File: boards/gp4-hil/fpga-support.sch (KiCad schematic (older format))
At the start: 0 parts

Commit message: Continued work on gp4-hil board schematic
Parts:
- added U2: XC7A100T-1FTG256C, symbol XC7AxT-xFTG256x
- added U6: W25Q32FW, symbol W25Q80BV
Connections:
- new net: U2.A16 (VCCO_15), U2.B13 (VCCO_15), U2.C10 (VCCO_15), U2.E14 (VCCO_15), U2.H15 (VCCO_15), U2.J12 (VCCO_15)
- new net: U2.A6 (VCCO_35), U2.B3 (VCCO_35), U2.D7 (VCCO_35), U2.E4 (VCCO_35), U2.F1 (VCCO_35), U2.J2 (VCCO_35)
- new net: U2.E10 (VCCBRAM), U2.F11 (VCCBRAM)
- new net: U2.F7 (VCCINT), U2.F9 (VCCINT), U2.G6 (VCCINT), U2.H9 (VCCINT), U2.J6 (VCCINT), U2.K9 (VCCINT), U2.L8 (VCCINT)
- new net: U2.G10 (VCCAUX), U2.J10 (VCCAUX), U2.K11 (VCCAUX), U2.L10 (VCCAUX)
- new net: U2.L16 (VCCO_14), U2.M13 (VCCO_14), U2.N10 (VCCO_14), U2.P7 (VCCO_14), U2.R14 (VCCO_14), U2.T11 (VCCO_14)
- new net: U2.M3 (VCCO_34), U2.R4 (VCCO_34), U2.T1 (VCCO_34)
- new net GND: U2.A1 (GND), U2.A11 (GND), U2.B8 (GND), U2.C15 (GND), U2.C5 (GND), U2.D12 (GND), U2.D2 (GND), U2.E9 (GND), U2.F10 (GND), U2.F16 (GND), U2.F6 (GND), U2.G13 (GND), U2.G3 (GND), U2.G7 (GNDADC), U2.G9 (GND), U2.H6 (GND), U2.J11 (GND), U2.J9 (GND), U2.K14 (GND), U2.K4 (GND), U2.K6 (GND), U2.L1 (GND), U2.L11 (GND), U2.M8 (GND), U2.N15 (GND), U2.N5 (GND), U2.P12 (GND), U2.P2 (GND), U2.R9 (GND), U2.T16 (GND), U2.T6 (GND)
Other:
- note added: "Recommended decoupling for 7a100t (largest FTG256 device):\n\nVCCINT\n* 1x 330 uF\n* 6x 4.7 uF\n* 8x 0.47 uF\n\nVCCBRAM\n* 1x 100 uF\n* 2x 0.47 uF\n\nVCCAUX\n* 1x 47 uF \n* 2x 4.7 uF \n* 3x 0.47 uF\n\nVCCO_0\n* 1x 47 uF\n\nVCCO (per bank):\n* 1x 47/100 uF per 4 banks\n* 2x 4.7 uF\n* 4x 0.47 uF"
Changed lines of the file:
@@
 EELAYER 25 0
 EELAYER END
-$Descr A4 11693 8268
+$Descr A3 16535 11693
 encoding utf-8
-Sheet 1 7
+Sheet 7 7
 Title ""
-Date ""
+Date "2016-05-10"
 Rev ""
 Comp ""
@@
 Comment4 ""
 $EndDescr
+$Comp
+L XC7AxT-xFTG256x U2
+U 1 1 5732CCFA
+P 1900 6200
+F 0 "U2" H 1900 6000 60  0000 L CNN
+F 1 "XC7A100T-1FTG256C" H 1900 6100 60  0000 L CNN
+F 2 "" H 1900 6200 60  0000 C CNN
+F 3 "" H 1900 6200 60  0000 C CNN
+	1    1900 6200
+	1    0    0    -1
+$EndComp
+$Comp
+L XC7AxT-xFTG256x U2
+U 2 1 5732CEE7
+P 5300 6200
+F 0 "U2" H 5300 6000 60  0000 L CNN
+F 1 "XC7A100T-1FTG256C" H 5300 6100 60  0000 L CNN
+F 2 "" H 5300 6200 60  0000 C CNN
+F 3 "" H 5300 6200 60  0000 C CNN
+	2    5300 6200
+	1    0    0    -1
+$EndComp
+$Comp
+L W25Q80BV U6
+U 1 1 5732D74D
+P 12400 4150
+F 0 "U6" H 12400 4837 60  0000 C CNN
+F 1 "W25Q32FW" H 12400 4731 60  0000 C CNN
+F 2 "" H 12400 4150 60  0000 C CNN
+F 3 "" H 12400 4150 60  0000 C CNN
+	1    12400 4150
+	1    0    0    -1
+$EndComp
+Text Notes 7450 9100 0    60   ~ 0
+Recommended decoupling for 7a100t (largest FTG256 device):\n\nVCCINT\n* 1x 330 uF\n* 6x 4.7 uF\n* 8x 0.47 uF\n\nVCCBRAM\n* 1x 100 uF\n* 2x 0.47 uF\n\nVCCAUX\n* 1x 47 uF \n* 2x 4.7 uF \n* 3x 0.47 uF\n\nVCCO_0\n* 1x 47 uF\n\nVCCO (per bank):\n* 1x 47/100 uF per 4 banks\n* 2x 4.7 uF\n* 4x 0.47 uF
+Wire Wire Line
+	5100 1500 5000 1500
+Wire Wire Line
+	5000 1300 5000 4400
+Wire Wire Line
+	5000 1600 5100 1600
+Wire Wire Line
+	5000 1700 5100 1700
+Connection ~ 5000 1600
+Wire Wire Line
+	5000 1800 5100 1800
+Connection ~ 5000 1700
+Wire Wire Line
+	5000 1900 5100 1900
+Connection ~ 5000 1800
+Wire Wire Line
+	5000 2000 5100 2000
+Connection ~ 5000 1900
+Wire Wire Line
+	5000 2100 5100 2100
+Connection ~ 5000 2000
+Wire Wire Line
+	5000 2200 5100 2200
+Connection ~ 5000 2100
+Wire Wire Line
+	5000 2300 5100 2300
+Connection ~ 5000 2200
+Wire Wire Line
+	5000 2400 5100 2400
+Connection ~ 5000 2300
+Wire Wire Line
+	5000 2500 5100 2500
+Connection ~ 5000 2400
+Wire Wire Line
+	5000 2600 5100 2600
+Connection ~ 5000 2500
+Wire Wire Line
+	5000 2700 5100 2700
+Connection ~ 5000 2600
+Wire Wire Line
+	5000 2800 5100 2800
+Connection ~ 5000 2700
+Wire Wire Line
+	5000 2900 5100 2900
+Connection ~ 5000 2800
+Wire Wire Line
+	5000 3000 5100 3000
+Connection ~ 5000 2900
+Wire Wire Line
+	5000 3100 5100 3100
+Connection ~ 5000 3000
+Wire Wire Line
+	5000 3200 5100 3200
+Connection ~ 5000 3100
+Wire Wire Line
+	5000 3300 5100 3300
+Connection ~ 5000 3200
+Wire Wire Line
+	5000 3400 5100 3400
+Connection ~ 5000 3300
+Wire Wire Line
+	5000 3500 5100 3500
+Connection ~ 5000 3400
+Wire Wire Line
+	5000 3600 5100 3600
+Connection ~ 5000 3500
+Wire Wire Line
+	5000 3700 5100 3700
+Connection ~ 5000 3600
+Wire Wire Line
+	5000 3800 5100 3800
+Connection ~ 5000 3700
+Wire Wire Line
+	5000 3900 5100 3900
+Connection ~ 5000 3800
+Wire Wire Line
+	5000 4000 5100 4000
+Connection ~ 5000 3900
+Wire Wire Line
+	5000 4100 5100 4100
+Connection ~ 5000 4000
+Wire Wire Line
+	5000 4200 5100 4200
+Connection ~ 5000 4100
+Wire Wire Line
+	5000 4300 5100 4300
+Connection ~ 5000 4200
+Wire Wire Line
+	5000 4400 5100 4400
+Connection ~ 5000 4300
+Wire Wire Line
+	4850 1300 5100 1300
+Connection ~ 5000 1500
+Connection ~ 5000 1300
+Wire Wire Line
+	6850 1650 6950 1650
+Wire Wire Line
+	6950 1650 6950 2250
+Wire Wire Line
+	6950 1750 6850 1750
+Wire Wire Line
+	6950 1850 6850 1850
+Connection ~ 6950 1750
+Wire Wire Line
+	6950 1950 6850 1950
+Connection ~ 6950 1850
+Wire Wire Line
+	6950 2050 6850 2050
+Connection ~ 6950 1950
+Wire Wire Line
+	6950 2150 6850 2150
+Connection ~ 6950 2050
+Wire Wire Line
+	6950 2250 6850 2250
+Connection ~ 6950 2150
+Wire Wire Line
+	6850 2450 6950 2450
+Wire Wire Line
+	6950 2450 6950 2550
+Wire Wire Line
+	6950 2550 6850 2550
+Wire Wire Line
+	6850 2750 6950 2750
+Wire Wire Line
+	6950 2750 6950 3050
+Wire Wire Line
+	6950 2850 6850 2850
+Wire Wire Line
+	6950 2950 6850 2950
+Connection ~ 6950 2850
+Wire Wire Line
+	6950 3050 6850 3050
+Connection ~ 6950 2950
+Wire Wire Line
+	6850 3450 6950 3450
+Wire Wire Line
+	6950 3450 6950 3950
+Wire Wire Line
+	6950 3550 6850 3550
+Wire Wire Line
+	6950 3650 6850 3650
+Connection ~ 6950 3550
+Wire Wire Line
+	6950 3750 6850 3750
+Connection ~ 6950 3650
+Wire Wire Line
+	6950 3850 6850 3850
+Connection ~ 6950 3750
+Wire Wire Line
+	6950 3950 6850 3950
+Connection ~ 6950 3850
+Wire Wire Line
+	6850 4150 6950 4150
+Wire Wire Line
+	6950 4150 6950 4650
+Wire Wire Line
+	6950 4250 6850 4250
+Wire Wire Line
+	6950 4350 6850 4350
+Connection ~ 6950 4250
+Wire Wire Line
+	6950 4450 6850 4450
+Connection ~ 6950 4350
+Wire Wire Line
+	6950 4550 6850 4550
+Connection ~ 6950 4450
+Wire Wire Line
+	6950 4650 6850 4650
+Connection ~ 6950 4550
+Wire Wire Line
+	6850 4850 6950 4850
+Wire Wire Line
+	6950 4850 6950 5050
+Wire Wire Line
+	6950 4950 6850 4950
+Wire Wire Line
+	6950 5050 6850 5050
+Connection ~ 6950 4950
+Wire Wire Line
+	6850 5250 6950 5250
+Wire Wire Line
+	6950 5250 6950 5750
+Wire Wire Line
+	6950 5350 6850 5350
+Wire Wire Line
+	6950 5450 6850 5450
+Connection ~ 6950 5350
+Wire Wire Line
+	6950 5550 6850 5550
+Connection ~ 6950 5450
+Wire Wire Line
+	6950 5650 6850 5650
+Connection ~ 6950 5550
+Wire Wire Line
+	6950 5750 6850 5750
+Connection ~ 6950 5650
+Text HLabel 4850 1300 0    60   Input ~ 0
+GND
 $EndSCHEMATC

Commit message: Schematic entry for 1V0 PSU
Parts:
- added C100, C101, C102, C103, C104, C105, C106, C107, C108, C109, C110, C111, C112, C113, C114, C115, C67, C70, C73, C75, C77, C79, C80, C81, C82, C83, C84, C85, C86: 0.47 uF, symbol C
- added C63: 330 uF, symbol C
- added C64: 100 uF, symbol C
- added C65, C87, C88, C89, C90, C91: 47 uF, symbol C
- added C66, C68, C69, C71, C72, C74, C76, C78, C92, C93, C94, C95, C96, C97, C98, C99: 4.7 uF, symbol C
- added J2: XILINX_JTAG, symbol XILINX_JTAG
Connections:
- net GND: now also C100.2, C101.2, C102.2, C103.2, C104.2, C105.2, C106.2, C107.2, C108.2, C109.2, C110.2, C111.2, C112.2, C113.2, C114.2, C115.2, C63.2, C64.2, C65.2, C66.2, C67.2, C68.2, C69.2, C70.2, C71.2, C72.2, C73.2, C74.2, C75.2, C76.2, C77.2, C78.2, C79.2, C80.2, C81.2, C82.2, C83.2, C84.2, C85.2, C86.2, C87.2, C88.2, C89.2, C90.2, C91.2, C92.2, C93.2, C94.2, C95.2, C96.2, C97.2, C98.2, C99.2
- new net: C100.1, C104.1, C108.1, C112.1, C88.1, C92.1, C96.1
- new net: C101.1, C105.1, C109.1, C113.1, C89.1, C93.1, C97.1
- new net: C102.1, C106.1, C110.1, C114.1, C90.1, C94.1, C98.1
- new net: C103.1, C107.1, C111.1, C115.1, C91.1, C95.1, C99.1
- new net 1V0: C63.1, C64.1, C66.1, C67.1, C69.1, C70.1, C72.1, C74.1, C76.1, C78.1, C79.1, C80.1, C81.1, C82.1, C83.1, C84.1, C85.1, C86.1
- new net 1V8: C65.1, C68.1, C71.1, C73.1, C75.1, C77.1
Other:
- note added: "VCCAUX decoupling"
- note added: "VCCBRAM decoupling"
- note added: "VCCINT decoupling"
- note added: "VCCO_0 decoupling"
- note added: "VCCO_14 decoupling"
- note added: "VCCO_15 decoupling"
- note added: "VCCO_34 decoupling"
- note added: "VCCO_35 decoupling"
- note removed: "Recommended decoupling for 7a100t (largest FTG256 device):\n\nVCCINT\n* 1x 330 uF\n* 6x 4.7 uF\n* 8x 0.47 uF\n\nVCCBRAM\n* 1x 100 uF\n* 2x 0.47 uF\n\nVCCAUX\n* 1x 47 uF \n* 2x 4.7 uF \n* 3x 0.47 uF\n\nVCCO_0\n* 1x 47 uF\n\nVCCO (per bank):\n* 1x 47/100 uF per 4 banks\n* 2x 4.7 uF\n* 4x 0.47 uF"
- moved on the sheet: U2A, U2B, U6

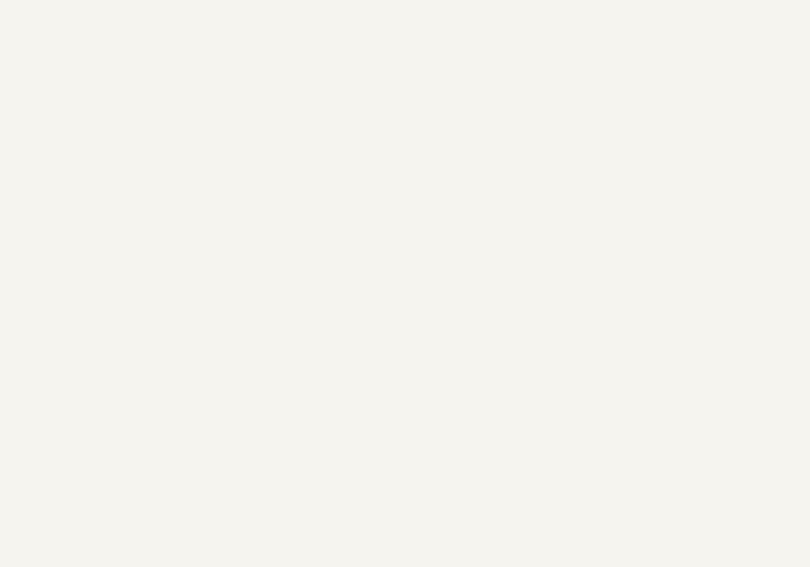
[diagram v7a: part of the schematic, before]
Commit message: Added load switches for DUT_VDDx rails
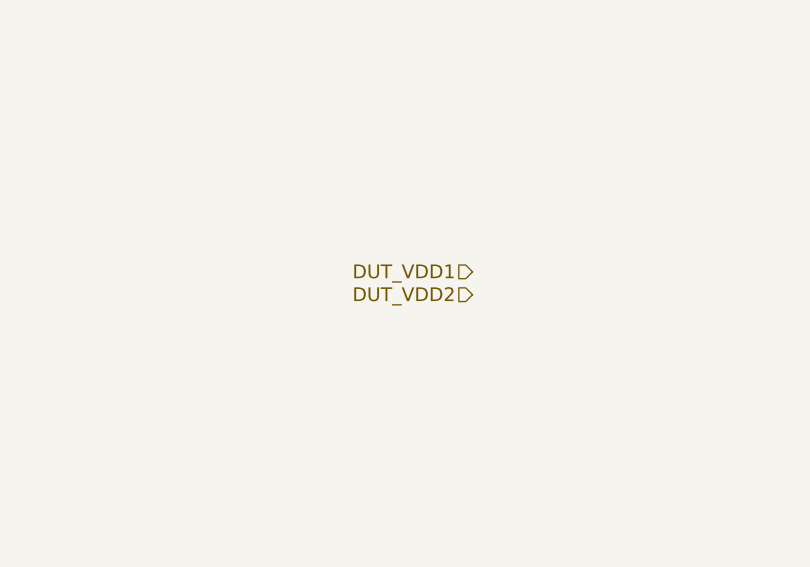
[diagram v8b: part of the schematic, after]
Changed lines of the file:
@@
 	1    0    0    -1
 $EndComp
+Text HLabel 13000 3750 0    60   Input ~ 0
+DUT_VDD1
+Text HLabel 13000 3850 0    60   Input ~ 0
+DUT_VDD2
 $EndSCHEMATC
